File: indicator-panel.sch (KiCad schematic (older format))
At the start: 77 parts, among them J101 Power In (5 - 12V), J102 GND, J103 GND, P101 Data in, P102 Data Out, P103 Power, P104 Power, U101 MAX3094E, U102 STP16CP05, U103 STP16CP05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

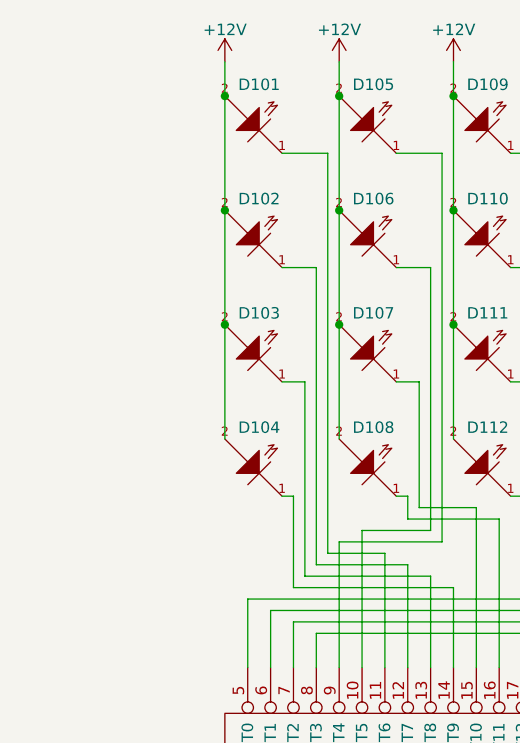
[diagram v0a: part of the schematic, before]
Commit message: Added fiducials
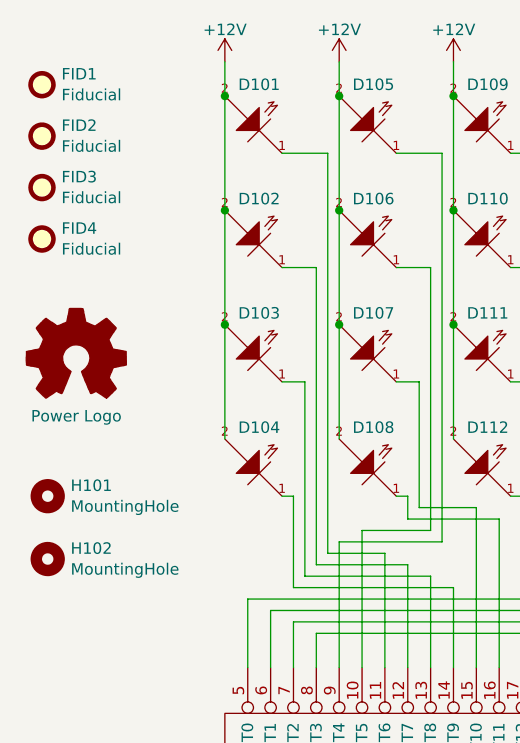
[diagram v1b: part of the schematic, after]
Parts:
- added FID1, FID2, FID3, FID4: Fiducial, Fiducial:Fiducial_1mm_Mask2mm, symbol Mechanical:Fiducial
- added H101, H102: MountingHole, MountingHole:MountingHole_3.5mm, symbol Mechanical:MountingHole
- added PowerLogo1: Power Logo, myMods:Barrel, symbol Graphic:Logo_Open_Hardware_Small
- J101: footprint myMods.pretty:PJ-032B -> myMods:PJ-032B
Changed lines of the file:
@@
 EESchema Schematic File Version 4
-LIBS:indicator-panel-cache
-EELAYER 26 0
+EELAYER 30 0
 EELAYER END
 $Descr USLetter 8500 11000 portrait
@@
 F 0 "J101" H 2000 8300 60  0000 C CNN
 F 1 "Power In (5 - 12V)" H 2000 7850 60  0000 C CNN
-F 2 "myMods.pretty:PJ-032B" H 2000 8050 60  0001 C CNN
+F 2 "myMods:PJ-032B" H 2000 8050 60  0001 C CNN
 F 3 "" H 2000 8050 60  0000 C CNN
 F 4 "PJ-032B" H 2000 8050 60  0001 C CNN "manf#"
@@
 Wire Wire Line
 	7100 7200 7100 7550
+$Comp
+L Mechanical:Fiducial FID1
+U 1 1 5FC2A1A4
+P 750 900
+F 0 "FID1" H 835 946 50  0000 L CNN
+F 1 "Fiducial" H 835 855 50  0000 L CNN
+F 2 "Fiducial:Fiducial_1mm_Mask2mm" H 750 900 50  0001 C CNN
+F 3 "~" H 750 900 50  0001 C CNN
+	1    750  900
+	1    0    0    -1
+$EndComp
+$Comp
+L Mechanical:Fiducial FID2
+U 1 1 5FC40805
+P 750 1125
+F 0 "FID2" H 835 1171 50  0000 L CNN
+F 1 "Fiducial" H 835 1080 50  0000 L CNN
+F 2 "Fiducial:Fiducial_1mm_Mask2mm" H 750 1125 50  0001 C CNN
+F 3 "~" H 750 1125 50  0001 C CNN
+	1    750  1125
+	1    0    0    -1
+$EndComp
+$Comp
+L Mechanical:Fiducial FID3
+U 1 1 5FC40B3B
+P 750 1350
+F 0 "FID3" H 835 1396 50  0000 L CNN
+F 1 "Fiducial" H 835 1305 50  0000 L CNN
+F 2 "Fiducial:Fiducial_1mm_Mask2mm" H 750 1350 50  0001 C CNN
+F 3 "~" H 750 1350 50  0001 C CNN
+	1    750  1350
+	1    0    0    -1
+$EndComp
+$Comp
+L Mechanical:Fiducial FID4
+U 1 1 5FC40FA2
+P 750 1575
+F 0 "FID4" H 835 1621 50  0000 L CNN
+F 1 "Fiducial" H 835 1530 50  0000 L CNN
+F 2 "Fiducial:Fiducial_1mm_Mask2mm" H 750 1575 50  0001 C CNN
+F 3 "~" H 750 1575 50  0001 C CNN
+	1    750  1575
+	1    0    0    -1
+$EndComp
+$Comp
+L Graphic:Logo_Open_Hardware_Small PowerLogo1
+U 1 1 5FC4613B
+P 900 2100
+F 0 "PowerLogo1" H 900 2375 50  0001 C CNN
+F 1 "Power Logo" H 900 1850 50  0000 C CNN
+F 2 "myMods:Barrel" H 900 2100 50  0001 C CNN
+F 3 "~" H 900 2100 50  0001 C CNN
+	1    900  2100
+	1    0    0    -1
+$EndComp
+$Comp
+L Mechanical:MountingHole H101
+U 1 1 5FC4F784
+P 775 2700
+F 0 "H101" H 875 2746 50  0000 L CNN
+F 1 "MountingHole" H 875 2655 50  0000 L CNN
+F 2 "MountingHole:MountingHole_3.5mm" H 775 2700 50  0001 C CNN
+F 3 "~" H 775 2700 50  0001 C CNN
+	1    775  2700
+	1    0    0    -1
+$EndComp
+$Comp
+L Mechanical:MountingHole H102
+U 1 1 5FC50D54
+P 775 2975
+F 0 "H102" H 875 3021 50  0000 L CNN
+F 1 "MountingHole" H 875 2930 50  0000 L CNN
+F 2 "MountingHole:MountingHole_3.5mm" H 775 2975 50  0001 C CNN
+F 3 "~" H 775 2975 50  0001 C CNN
+	1    775  2975
+	1    0    0    -1
+$EndComp
 $EndSCHEMATC
